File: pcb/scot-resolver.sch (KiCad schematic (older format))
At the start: 32 parts

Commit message: WIP PCB (starting layout)
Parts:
- removed C? (x7): 1u, symbol Device:C
- removed C?: 10u, symbol Device:C
- removed C?: 10n, symbol Device:C
- removed C?: 4u7, symbol Device:C
- removed C? (x2): 100n, symbol Device:C
- removed D?: D, symbol Device:D
- removed FB? (x2): Ferrite_Bead, symbol Device:Ferrite_Bead
- removed IC?: MCP2562, agg:DFN-8-EP-MICROCHIP, symbol agg-kicad:MCP2562
- removed IC?: TSR1, agg:TSR1, symbol agg-kicad:TSR1
- removed IC?: STM32F0xxKxTx, agg:LQFP-32, symbol agg-kicad:STM32F0xxKxTx
- removed J? (x4): Conn_01x02_Female, symbol Connector:Conn_01x02_Female
- removed P?: SWD, agg:FTSH-105-01-F-D-K, symbol agg-kicad:SWD
- removed R?: 120R, symbol Device:R
- removed R? (x2): R, symbol Device:R
- removed U?: MCP1703A-5002_SOT223, Package_TO_SOT_SMD:SOT-223-3_TabPin2, symbol Regulator_Linear:MCP1703A-5002_SOT223
- removed U?: LT1762, Package_SO:MSOP-8_3x3mm_P0.65mm, symbol Regulator_Linear:LT1762
- removed U?: MCP1703A-3302_SOT223, Package_TO_SOT_SMD:SOT-223-3_TabPin2, symbol Regulator_Linear:MCP1703A-3302_SOT223
- removed Y?: XTAL, symbol agg-kicad:XTAL
- added J1: Conn_01x02_Female, TerminalBlock_TE-Connectivity:TerminalBlock_TE_282834-2_1x02_P2.54mm_Horizontal, symbol Connector:Conn_01x02_Female
- added J4, J5, J6: Conn_01x03_Female, TerminalBlock_TE-Connectivity:TerminalBlock_TE_282834-3_1x03_P2.54mm_Horizontal, symbol Connector:Conn_01x03_Female
- J2, J3: renamed from J?; footprint (none) -> TerminalBlock_TE-Connectivity:TerminalBlock_TE_282834-2_1x02_P2.54mm_Horizontal
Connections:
- net CAN TXRX/CAN_L: now reaches J2.1 (Pin_1), J3.1 (Pin_1)
- net CAN TXRX/CAN_H: now reaches J2.2 (Pin_2), J3.2 (Pin_2)
- new net GNDA: J4.1 (Pin_1), J5.1 (Pin_1), J6.1 (Pin_1)
- new net Power Supplies/POWER_28V+: J1.2 (Pin_2)
- new net Power Supplies/POWER_28V-: J1.1 (Pin_1)
- new net Resolver Exciter/EXC+_OUTPUT: J4.3 (Pin_3)
- new net Resolver Exciter/EXC-_OUTPUT: J4.2 (Pin_2)
- new net Resolver Receiver COS+/RECEIVER_INPUT: J6.3 (Pin_3)
- new net Resolver Receiver COS-/RECEIVER_INPUT: J6.2 (Pin_2)
- new net Resolver Receiver SIN+/RECEIVER_INPUT: J5.3 (Pin_3)
- new net Resolver Receiver SIN-/RECEIVER_INPUT: J5.2 (Pin_2)
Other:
- note added: "Orange & Block Powerpole Connector"
- note added: "Resolver Cosine Receiver Coil"
- note added: "Resolver Exciter Coil"
- note added: "Resolver Sine Receiver Coil"
- note removed: "12V"
- note removed: "15V"
- note removed: "28V"
- note removed: "28V Powerpole"
- note removed: "28VDC -> 15VDC Power Input"
- moved on the sheet: J2, J3

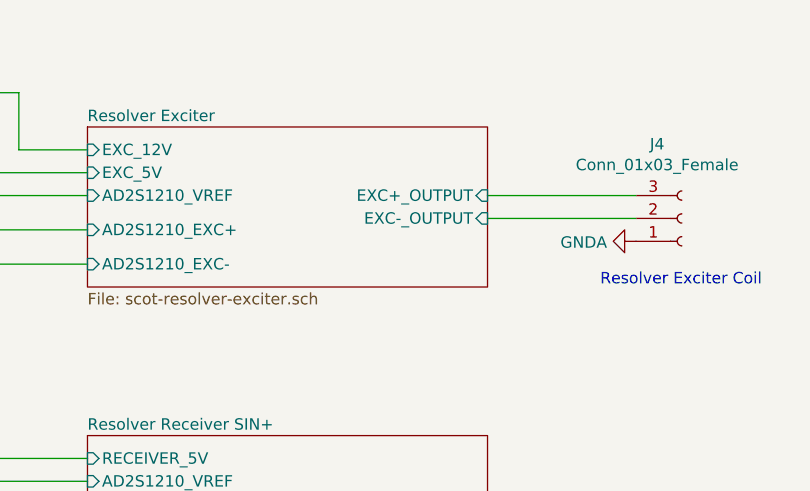
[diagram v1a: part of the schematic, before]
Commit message: PCB Progress, laying tracks.
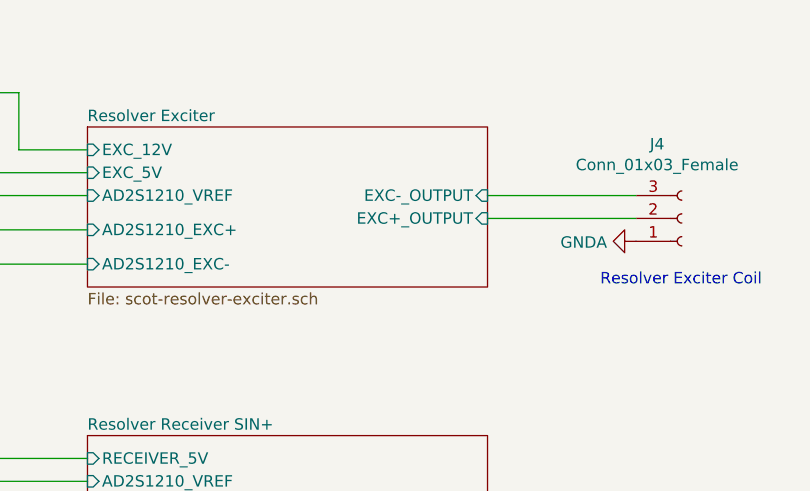
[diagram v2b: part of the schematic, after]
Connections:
- net Resolver Exciter/EXC+_OUTPUT: now also J4.2 (Pin_2); no longer J4.3 (Pin_3)
- net Resolver Exciter/EXC-_OUTPUT: now also J4.3 (Pin_3); no longer J4.2 (Pin_2)
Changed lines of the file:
@@
 F1 "scot-resolver-exciter.sch" 50
 F2 "AD2S1210_VREF" I L 7550 1550 50
-F3 "EXC+_OUTPUT" I R 9300 1550 50
-F4 "EXC-_OUTPUT" I R 9300 1650 50
+F3 "EXC+_OUTPUT" I R 9300 1650 50
+F4 "EXC-_OUTPUT" I R 9300 1550 50
 F5 "AD2S1210_EXC+" I L 7550 1700 50
 F6 "AD2S1210_EXC-" I L 7550 1850 50

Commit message: WIP (nearly there!)
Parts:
- added H1, H2: MountingHole, agg:M3_MOUNT, symbol Mechanical:MountingHole
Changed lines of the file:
@@
 	1    0    0    1
 $EndComp
+$Comp
+L Mechanical:MountingHole H1
+U 1 1 5E4FCB16
+P 5400 900
+F 0 "H1" H 5500 946 50  0000 L CNN
+F 1 "MountingHole" H 5500 855 50  0000 L CNN
+F 2 "agg:M3_MOUNT" H 5400 900 50  0001 C CNN
+F 3 "~" H 5400 900 50  0001 C CNN
+	1    5400 900
+	1    0    0    -1
+$EndComp
+$Comp
+L Mechanical:MountingHole H2
+U 1 1 5E4FD6C4
+P 5550 4950
+F 0 "H2" H 5650 4996 50  0000 L CNN
+F 1 "MountingHole" H 5650 4905 50  0000 L CNN
+F 2 "agg:M3_MOUNT" H 5550 4950 50  0001 C CNN
+F 3 "~" H 5550 4950 50  0001 C CNN
+	1    5550 4950
+	1    0    0    -1
+$EndComp
 $EndSCHEMATC

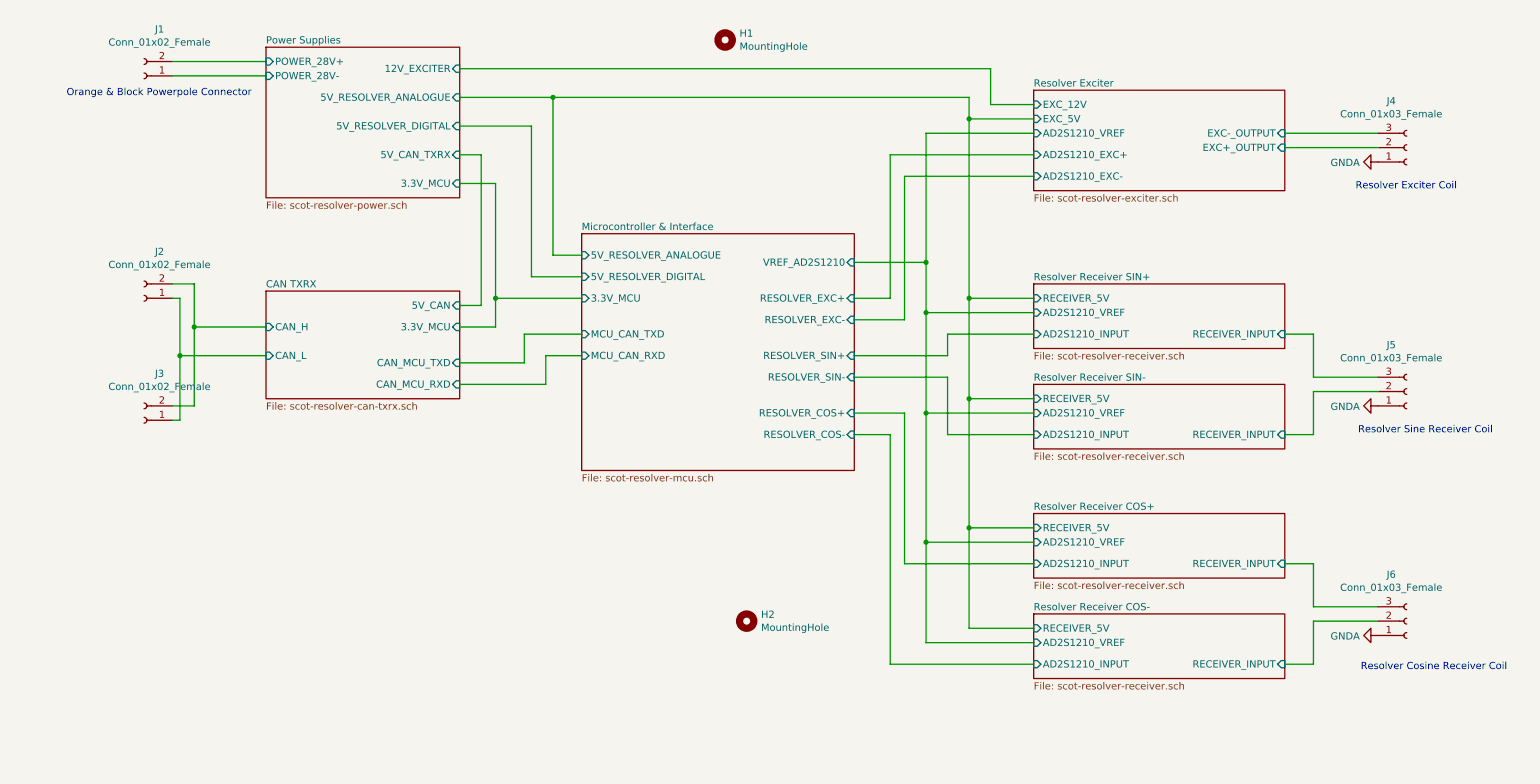
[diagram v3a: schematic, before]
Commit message: pcb: Add labels and values to schematic.
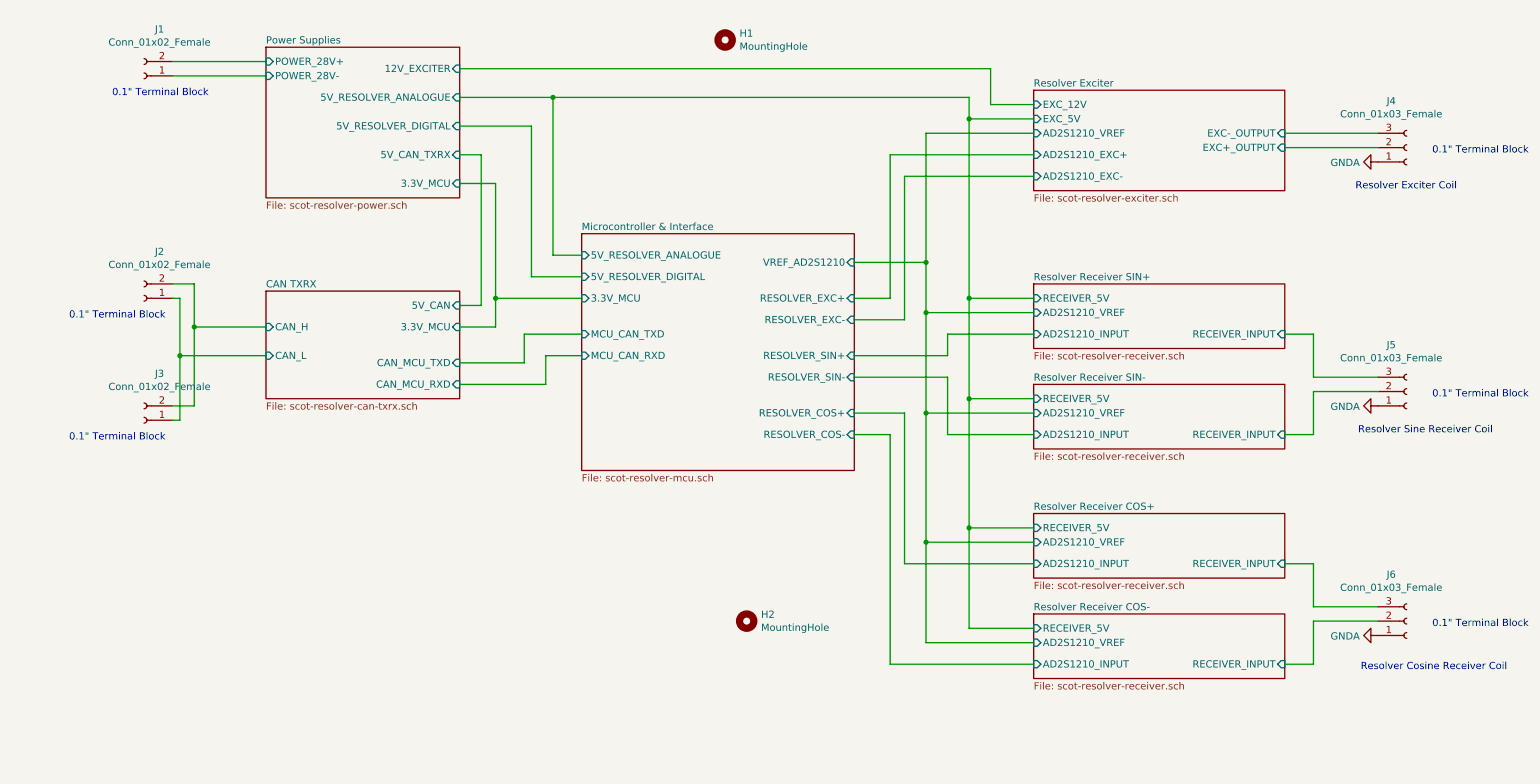
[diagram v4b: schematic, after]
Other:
- note added: "0.1" Terminal Block"
- note removed: "Orange & Block Powerpole Connector"
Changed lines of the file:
@@
 Wire Wire Line
 	6650 2850 6300 2850
-Text Notes 2100 1300 2    50   ~ 0
-Orange & Block Powerpole Connector
+Text Notes 1800 1300 2    50   ~ 0
+0.1" Terminal Block
 Text Notes 10500 1950 2    50   ~ 0
 Resolver Exciter Coil
@@
 	1    0    0    -1
 $EndComp
+Text Notes 1500 2850 2    50   ~ 0
+0.1" Terminal Block
+Text Notes 1500 3700 2    50   ~ 0
+0.1" Terminal Block
+Text Notes 11000 1700 2    50   ~ 0
+0.1" Terminal Block
+Text Notes 11000 3400 2    50   ~ 0
+0.1" Terminal Block
+Text Notes 11000 5000 2    50   ~ 0
+0.1" Terminal Block
 $EndSCHEMATC

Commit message: WIP PCB v2.
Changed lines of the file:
@@
 F0 "Power Supplies" 50
 F1 "scot-resolver-power.sch" 50
-F2 "12V_EXCITER" I R 3550 1100 50
-F3 "POWER_28V+" I L 2200 1050 50
-F4 "POWER_28V-" I L 2200 1150 50
-F5 "5V_CAN_TXRX" I R 3550 1700 50
-F6 "3.3V_MCU" I R 3550 1900 50
-F7 "5V_RESOLVER_DIGITAL" I R 3550 1500 50
-F8 "5V_RESOLVER_ANALOGUE" I R 3550 1300 50
+F2 "POWER_28V+" I L 2200 1050 50
+F3 "POWER_28V-" I L 2200 1150 50
+F4 "EXCITER_16V+" I R 3550 1050 50
+F5 "0V_EXCITER" I R 3550 1150 50
+F6 "3.3V_MCU" I R 3550 1850 50
+F7 "5V_CAN_TXRX" I R 3550 1700 50
+F8 "5V_RESOLVER_DIGITAL" I R 3550 1550 50
+F9 "5V_RESOLVER_ANALOGUE" I R 3550 1300 50
+F10 "0V_ANALOG" I R 3550 1400 50
+F11 "0V_DIGITAL" I R 3550 1950 50
 $EndSheet
 $Comp
@@
 	3800 2900 3800 2700
 Wire Wire Line
-	3800 1900 3550 1900
+	3800 1850 3550 1850
 Wire Wire Line
 	3550 1700 3700 1700
@@
 	3700 2750 3550 2750
 Wire Wire Line
-	3550 1100 7250 1100
-Wire Wire Line
-	7250 1100 7250 1350
+	3550 1050 7250 1050
+Wire Wire Line
+	7250 1050 7250 1350
 Wire Wire Line
 	7250 1350 7550 1350
@@
 Connection ~ 3800 2700
 Wire Wire Line
-	3800 2700 3800 1900
+	3800 2700 3800 1850
 Wire Wire Line
 	4400 2950 4000 2950
@@
 	4400 2550 4050 2550
 Wire Wire Line
-	4050 2550 4050 1500
-Wire Wire Line
-	4050 1500 3550 1500
+	4050 2550 4050 1550
+Wire Wire Line
+	4050 1550 3550 1550
 $Comp
 L power:GNDA #PWR0101
